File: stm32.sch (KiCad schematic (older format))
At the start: 46 parts, among them P1 USB_OTG, P2 CONN_01X04, U3 STM32F407VETx, U4 USBLC6-4SC6, Y2 25M

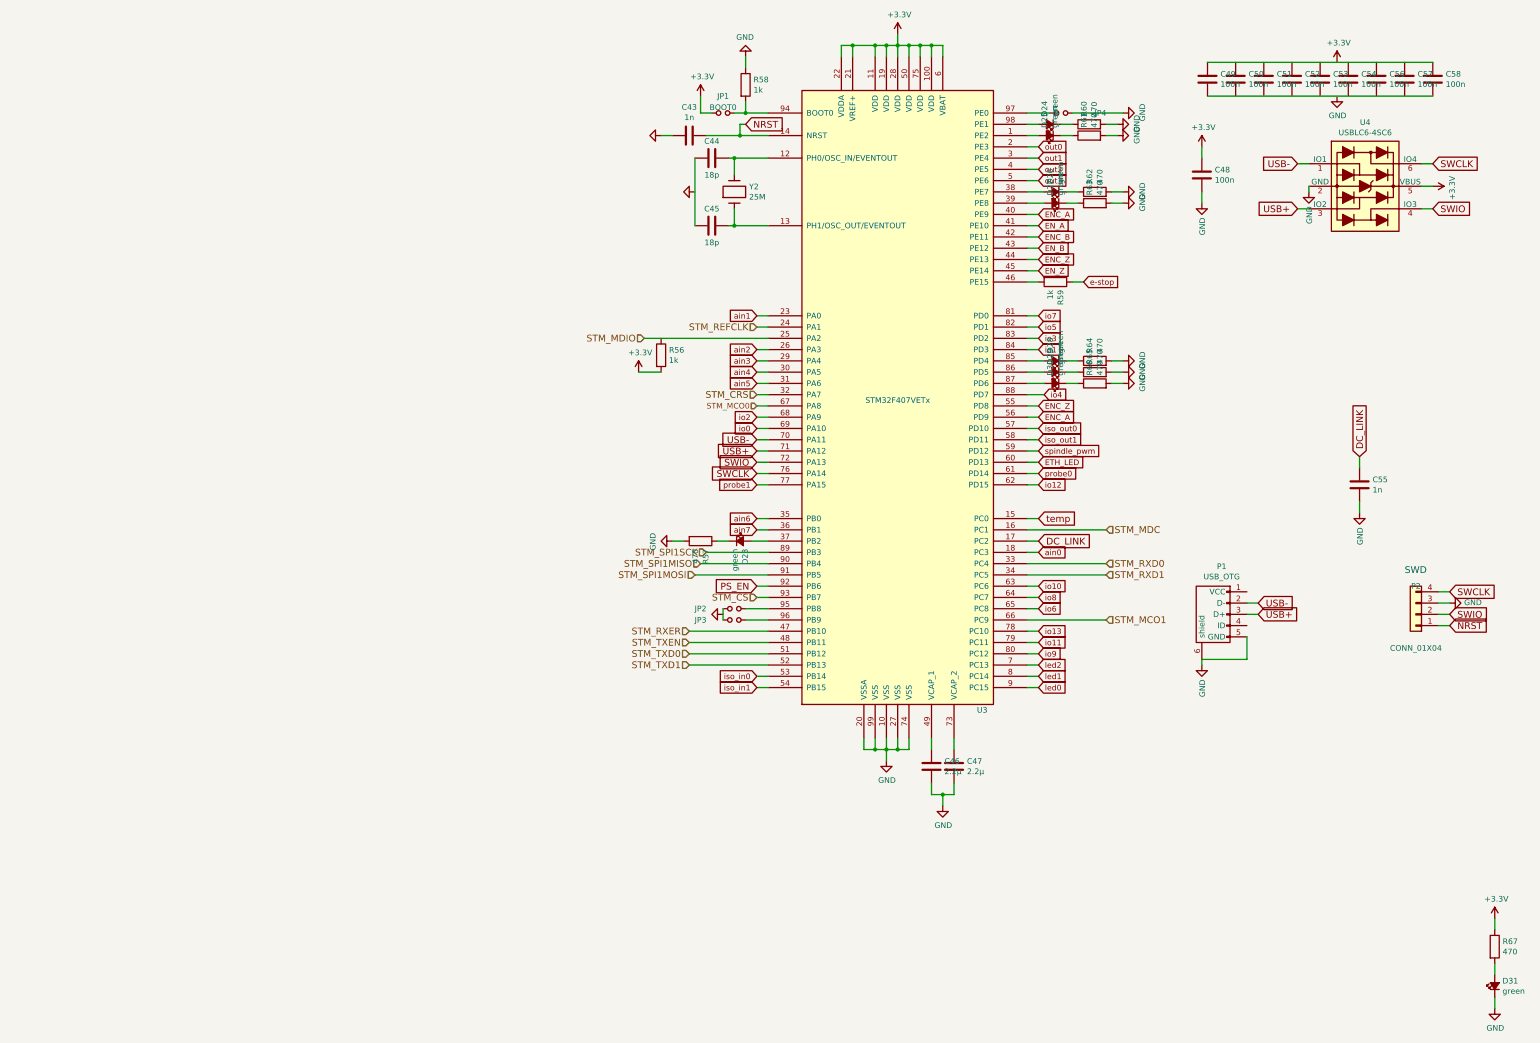
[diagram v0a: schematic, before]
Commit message: remove xfmrs from top board, no space with 18650 backup battery
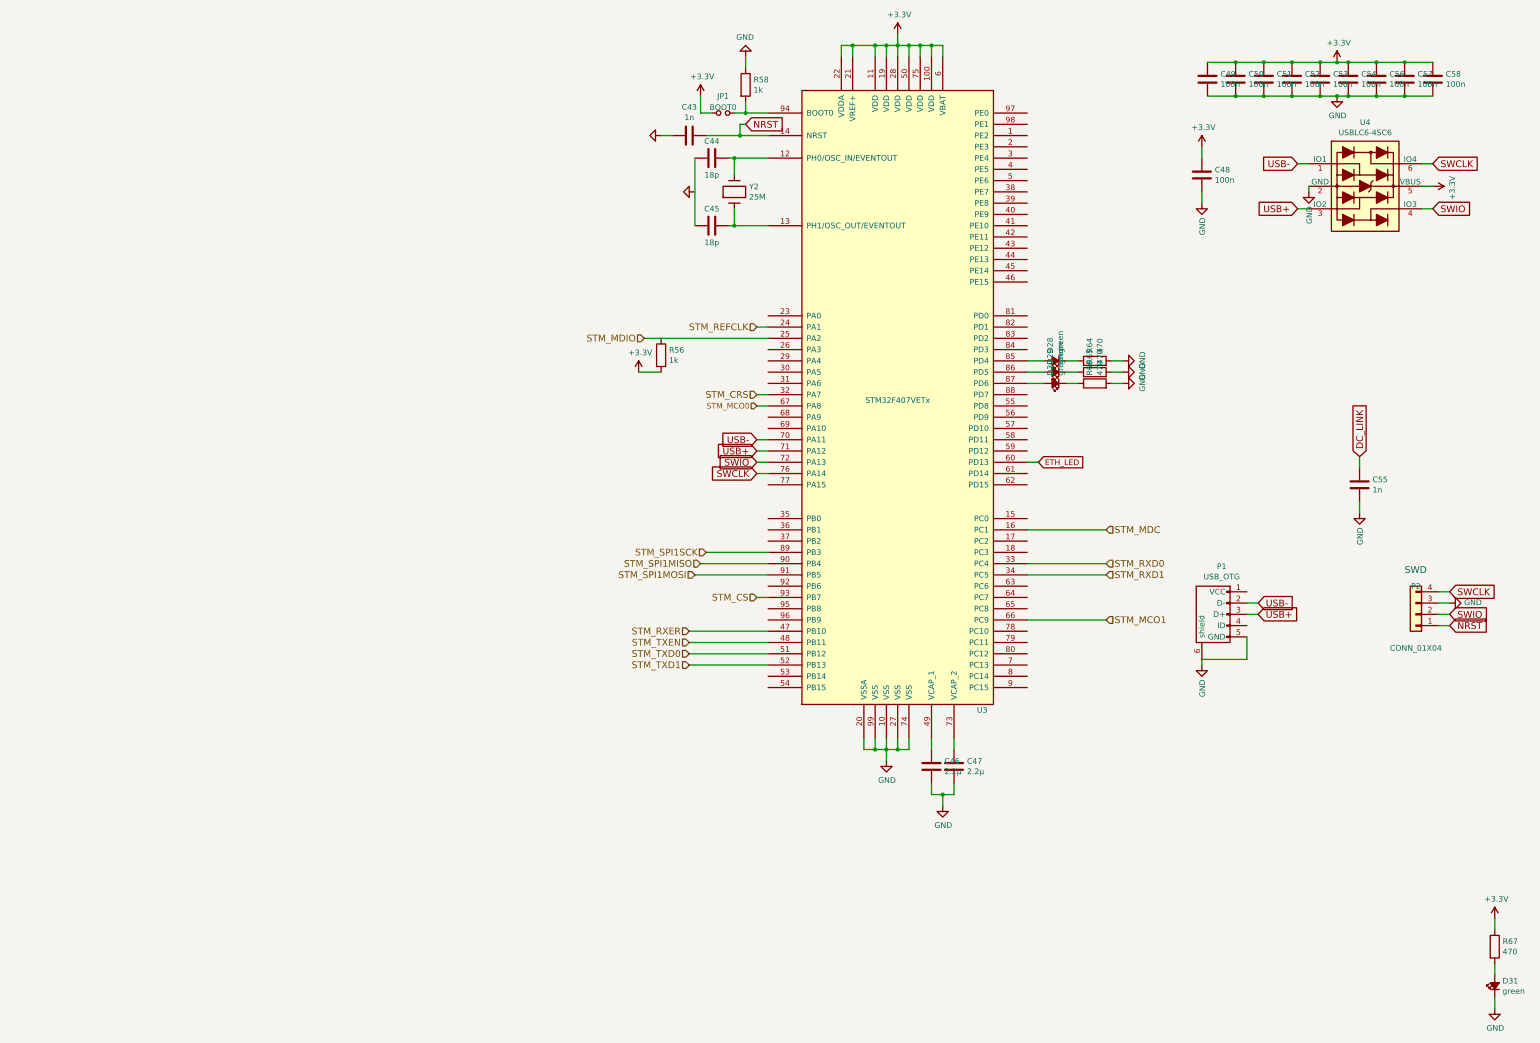
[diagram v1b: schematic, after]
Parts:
- removed D23, D24, D25, D26, D27: green, stmbl:LED-0805, symbol stmbl:Led_Small
- removed JP2, JP3, JP4: Jumper, stmbl:SOLDER_JUMPER, symbol stmbl:Jumper_NO_Small
- removed R57, R60, R61, R62, R63: 470, stmbl:R_0603, symbol stmbl:R
- removed R59: 1k, stmbl:R_0603, symbol stmbl:R
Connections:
- net +3V3: now also C49.2, C50.2, C51.2, C52.2, C53.2, C54.2, C56.2, C57.2, C58.2
- net DC_LINK: no longer U3.17 (PC2)
- net GND: now also C49.1, C50.1, C51.1, C52.1, C53.1, C54.1, C56.1, C57.1, C58.1
- net ENC_A: no longer names the net of U3.40 (PE9)
- net ENC_A: no longer U3.56 (PD9)
- net ENC_B: no longer names the net of U3.42 (PE11)
- net ENC_Z: no longer names the net of U3.44 (PE13)
- net ENC_Z: no longer U3.55 (PD8)
- net EN_A: no longer names the net of U3.41 (PE10)
- net EN_B: no longer names the net of U3.43 (PE12)
- net EN_Z: no longer names the net of U3.45 (PE14)
- net PS_EN: no longer names the net of U3.92 (PB6)
- net ain0: no longer names the net of U3.18 (PC3)
- net ain1: no longer names the net of U3.23 (PA0)
- net ain2: no longer names the net of U3.26 (PA3)
- net ain3: no longer names the net of U3.29 (PA4)
- net ain4: no longer names the net of U3.30 (PA5)
- net ain5: no longer names the net of U3.31 (PA6)
- net ain6: no longer names the net of U3.35 (PB0)
- net ain7: no longer names the net of U3.36 (PB1)
- net io0: no longer names the net of U3.69 (PA10)
- net io1: no longer names the net of U3.84 (PD3)
- net io10: no longer names the net of U3.63 (PC6)
- net io11: no longer names the net of U3.79 (PC11)
- net io12: no longer names the net of U3.62 (PD15)
- net io13: no longer names the net of U3.78 (PC10)
- net io2: no longer names the net of U3.68 (PA9)
- net io3: no longer names the net of U3.83 (PD2)
- net io4: no longer names the net of U3.88 (PD7)
- net io5: no longer names the net of U3.82 (PD1)
- net io6: no longer names the net of U3.65 (PC8)
- net io7: no longer names the net of U3.81 (PD0)
- net io8: no longer names the net of U3.64 (PC7)
- net io9: no longer names the net of U3.80 (PC12)
- net iso_in0: no longer names the net of U3.53 (PB14)
- net iso_in1: no longer names the net of U3.54 (PB15)
- net iso_out0: no longer names the net of U3.57 (PD10)
- net iso_out1: no longer names the net of U3.58 (PD11)
- net led0: no longer names the net of U3.9 (PC15)
- net led1: no longer names the net of U3.8 (PC14)
- net led2: no longer names the net of U3.7 (PC13)
- net out0: no longer names the net of U3.2 (PE3)
- net out1: no longer names the net of U3.3 (PE4)
- net out2: no longer names the net of U3.4 (PE5)
- net out3: no longer names the net of U3.5 (PE6)
- net probe0: no longer names the net of U3.61 (PD14)
- net probe1: no longer names the net of U3.77 (PA15)
- net spindle_pwm: no longer names the net of U3.59 (PD12)
- net temp: no longer names the net of U3.15 (PC0)

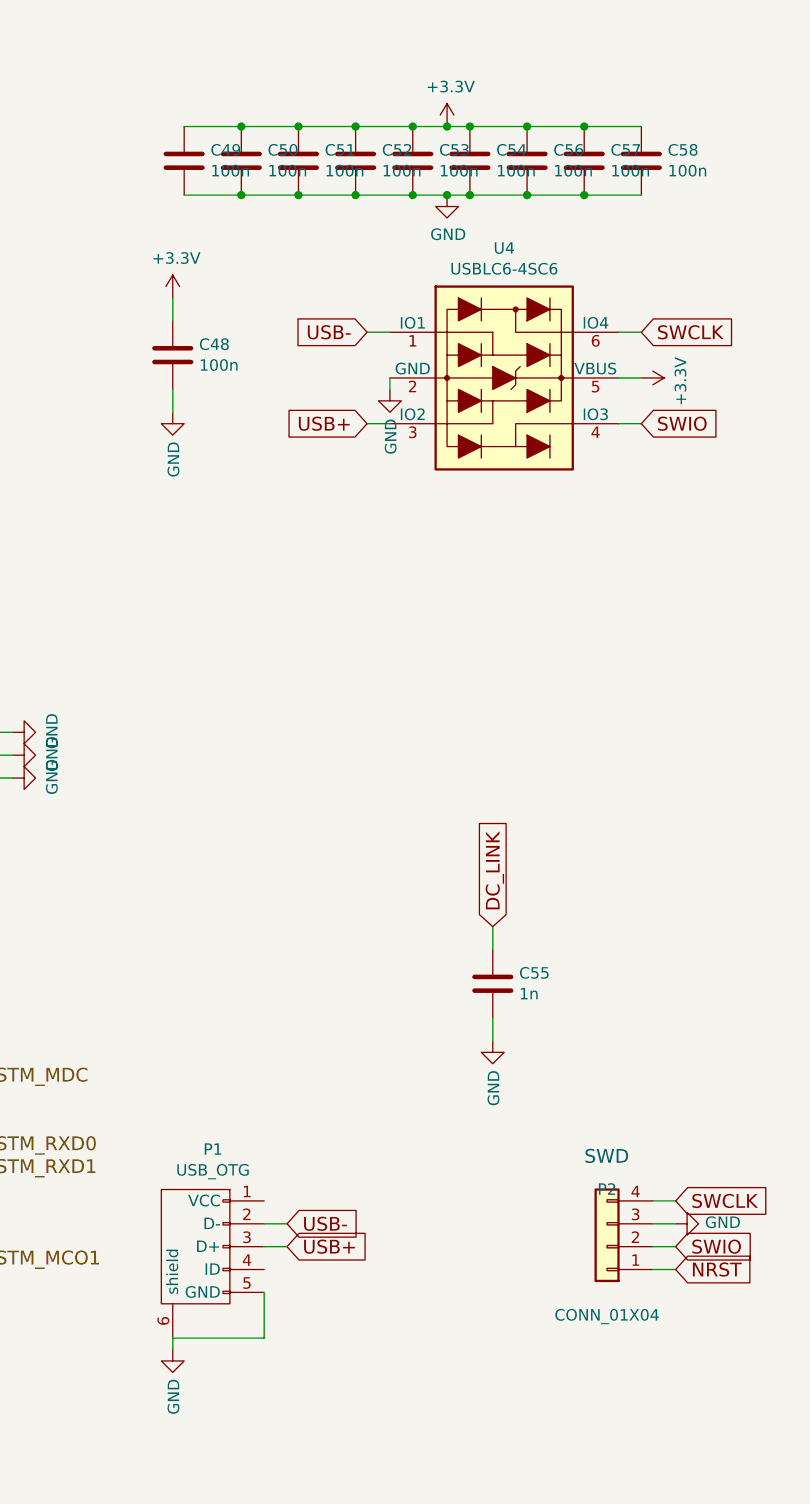
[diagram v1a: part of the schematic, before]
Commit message: Change to bigger housing
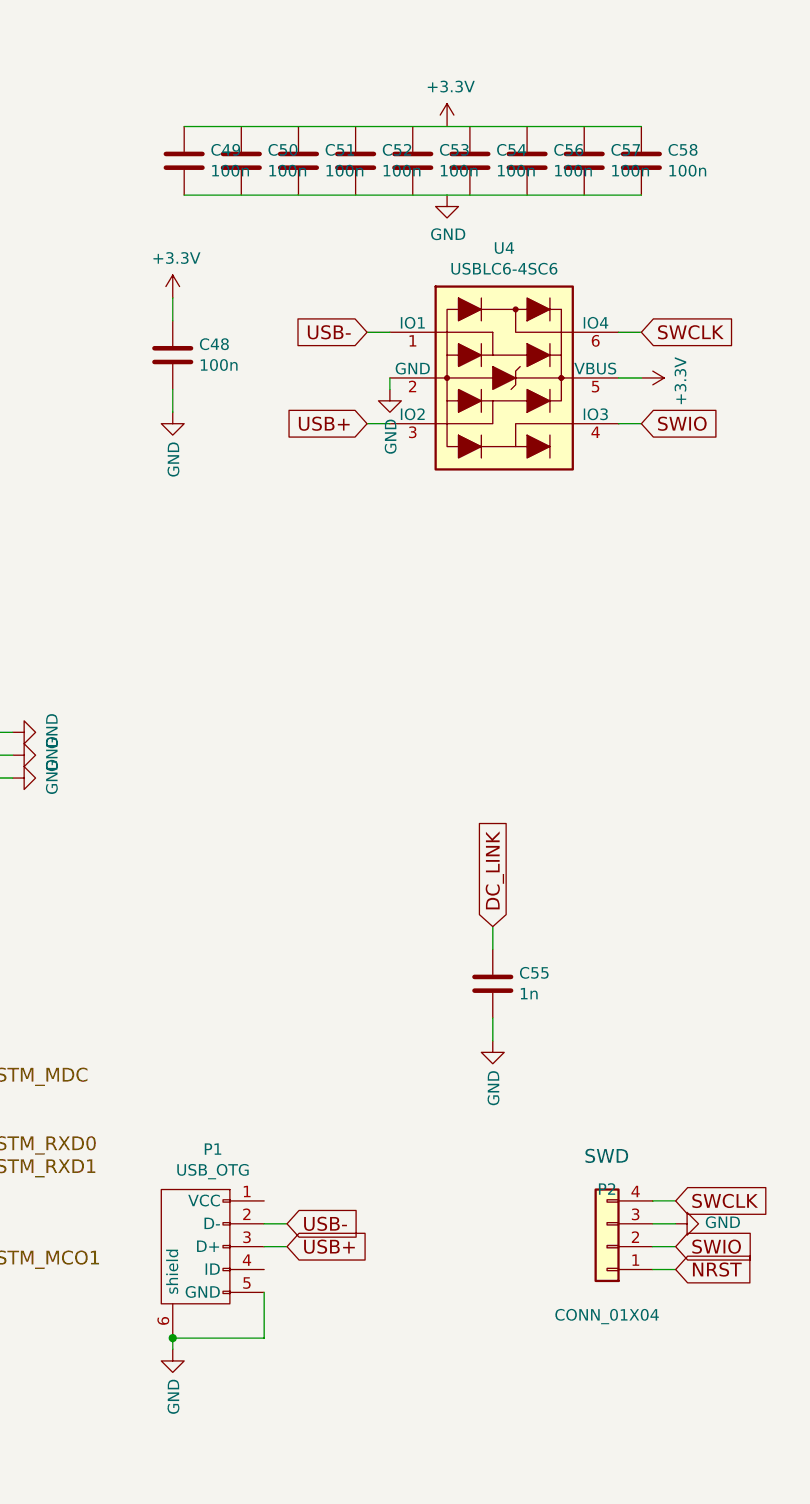
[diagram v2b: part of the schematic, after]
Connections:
- net +3V3: no longer C49.2, C50.2, C51.2, C52.2, C53.2, C54.2, C56.2, C57.2, C58.2
- net GND: no longer C49.1, C50.1, C51.1, C52.1, C53.1, C54.1, C56.1, C57.1, C58.1
- new net: C49.1, C58.1
- new net: C49.2, C58.2
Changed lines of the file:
@@
-EESchema Schematic File Version 4
+EESchema Schematic File Version 5
+LIBS:powermetering-cache
 EELAYER 29 0
 EELAYER END
@@
 	8300 1800 8300 2400
 Wire Wire Line
-	12850 950  13100 950
-Wire Wire Line
-	12850 1250 13100 1250
-Connection ~ 14600 950
-Wire Wire Line
-	14600 950  14850 950
-Connection ~ 14350 950
-Wire Wire Line
-	14350 950  14600 950
-Connection ~ 14100 950
-Wire Wire Line
-	14100 950  14350 950
-Connection ~ 14000 950
-Wire Wire Line
-	14000 950  14100 950
-Connection ~ 13850 950
-Wire Wire Line
-	13850 950  14000 950
-Connection ~ 13600 950
-Wire Wire Line
-	13600 950  13850 950
-Connection ~ 13350 950
-Wire Wire Line
-	13350 950  13600 950
-Connection ~ 13100 950
-Wire Wire Line
-	13100 950  13350 950
-Connection ~ 13100 1250
-Wire Wire Line
-	13100 1250 13350 1250
-Connection ~ 13350 1250
-Wire Wire Line
-	13350 1250 13600 1250
-Connection ~ 13600 1250
-Wire Wire Line
-	13600 1250 13850 1250
-Connection ~ 13850 1250
-Wire Wire Line
-	13850 1250 14000 1250
-Connection ~ 14000 1250
-Wire Wire Line
-	14000 1250 14100 1250
-Connection ~ 14100 1250
-Wire Wire Line
-	14100 1250 14350 1250
-Connection ~ 14350 1250
-Wire Wire Line
-	14350 1250 14600 1250
-Connection ~ 14600 1250
-Wire Wire Line
-	14600 1250 14850 1250
+	12850 1250 14850 1250
+Wire Wire Line
+	12850 950  14850 950
+Connection ~ 12800 6250
 $EndSCHEMATC

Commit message: add supply and AFE isolation
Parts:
- added Y3: RTC, stmbl:Crystal_SMD_0603_4Pads, symbol stmbl:Crystal
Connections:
- net +3V3: now also C49.2, C50.2, C51.2, C52.2, C53.2, C54.2, C56.2, C57.2, C58.2
- net GND: now also C49.1, C50.1, C51.1, C52.1, C53.1, C54.1, C56.1, C57.1, C58.1, Y3.1
- net STM_MDIO: now also R56.1
- net at U3.54 (PB15): now also Y3.2
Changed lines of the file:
@@
-EESchema Schematic File Version 5
+EESchema Schematic File Version 4
 LIBS:powermetering-cache
 EELAYER 29 0
@@
 $Descr A3 16535 11693
 encoding utf-8
-Sheet 3 4
+Sheet 3 3
 Title "STM32 Ethernet BOB"
 Date ""
@@
 Wire Wire Line
 	10400 900  10400 800
-Connection ~ 10400 800
-Wire Wire Line
-	10400 800  10500 800
 Wire Wire Line
 	10300 900  10300 800
@@
 	8400 5300 8950 5300
 Wire Wire Line
-	7850 3400 8950 3400
+	7850 3400 8000 3400
 Wire Wire Line
 	8300 1800 8300 2400
 Wire Wire Line
-	12850 1250 14850 1250
-Wire Wire Line
-	12850 950  14850 950
+	12850 1250 13100 1250
+Wire Wire Line
+	12850 950  13100 950
 Connection ~ 12800 6250
+$Comp
+L stmbl:Crystal Y3
+U 1 1 5D421BBB
+P 8950 6750
+F 0 "Y3" V 8996 6619 50  0000 R CNN
+F 1 "RTC" V 8905 6619 50  0000 R CNN
+F 2 "stmbl:Crystal_SMD_0603_4Pads" H 8950 6750 50  0001 C CNN
+F 3 "" H 8950 6750 50  0000 C CNN
+F 4 "LFXTAL061642Reel" H 300 4650 50  0001 C CNN "Manufacturer No"
+F 5 "Mouser 449-LFXTAL061642REEL" H 300 4650 50  0001 C CNN "Source"
+F 6 "" H 300 4650 50  0001 C CNN "Tolerance"
+F 7 "" H 300 4650 50  0001 C CNN "Voltage"
+	1    8950 6750
+	0    -1   -1   0
+$EndComp
+Wire Wire Line
+	8950 6500 8950 6600
+$Comp
+L stmbl:GND #PWR0161
+U 1 1 5D42CB08
+P 8950 7000
+F 0 "#PWR0161" H 8950 6750 50  0001 C CNN
+F 1 "GND" H 8955 6827 50  0000 C CNN
+F 2 "" H 8950 7000 50  0000 C CNN
+F 3 "" H 8950 7000 50  0000 C CNN
+	1    8950 7000
+	1    0    0    -1
+$EndComp
+Wire Wire Line
+	8950 7000 8950 6900
+Wire Wire Line
+	10500 800  10400 800
+Connection ~ 10400 800
+Connection ~ 14600 950
+Wire Wire Line
+	14600 950  14850 950
+Connection ~ 14350 950
+Wire Wire Line
+	14350 950  14600 950
+Connection ~ 14100 950
+Wire Wire Line
+	14100 950  14350 950
+Connection ~ 14000 950
+Wire Wire Line
+	14000 950  14100 950
+Connection ~ 13850 950
+Wire Wire Line
+	13850 950  14000 950
+Connection ~ 13600 950
+Wire Wire Line
+	13600 950  13850 950
+Connection ~ 13350 950
+Wire Wire Line
+	13350 950  13600 950
+Connection ~ 13100 950
+Wire Wire Line
+	13100 950  13350 950
+Connection ~ 13100 1250
+Wire Wire Line
+	13100 1250 13350 1250
+Connection ~ 13350 1250
+Wire Wire Line
+	13350 1250 13600 1250
+Connection ~ 13600 1250
+Wire Wire Line
+	13600 1250 13850 1250
+Connection ~ 13850 1250
+Wire Wire Line
+	13850 1250 14000 1250
+Connection ~ 14000 1250
+Wire Wire Line
+	14000 1250 14100 1250
+Connection ~ 14100 1250
+Wire Wire Line
+	14100 1250 14350 1250
+Connection ~ 14350 1250
+Wire Wire Line
+	14350 1250 14600 1250
+Connection ~ 14600 1250
+Wire Wire Line
+	14600 1250 14850 1250
+Connection ~ 8000 3400
+Wire Wire Line
+	8000 3400 8950 3400
 $EndSCHEMATC

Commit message: eth phy
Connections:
- net +3V3: now also D31.2 (A); no longer R67.1
- net GND: now also R67.2; no longer D31.1 (K)
- new net: D31.1 (K), R67.1
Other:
- moved on the sheet: D31, R67
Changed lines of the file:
@@
 L stmbl:Led_Small D31
 U 1 1 5B4CB472
-P 15400 9150
-F 0 "D31" V 15446 9082 50  0000 R CNN
-F 1 "green" V 15355 9082 50  0000 R CNN
-F 2 "stmbl:LED-0805" V 15400 9150 50  0001 C CNN
-F 3 "" V 15400 9150 50  0000 C CNN
-F 4 "LG R971" H 0   0   50  0001 C CNN "Manufacturer No"
-F 5 "Mouser 720-LGR971-KN-1" H 0   0   50  0001 C CNN "Source"
-F 6 "" H 0   0   50  0001 C CNN "Tolerance"
-F 7 "" H 0   0   50  0001 C CNN "Voltage"
-	1    15400 9150
+P 15400 8750
+F 0 "D31" V 15446 8682 50  0000 R CNN
+F 1 "green" V 15355 8682 50  0000 R CNN
+F 2 "stmbl:LED-0805" V 15400 8750 50  0001 C CNN
+F 3 "" V 15400 8750 50  0000 C CNN
+F 4 "LG R971" H 0   -400 50  0001 C CNN "Manufacturer No"
+F 5 "Mouser 720-LGR971-KN-1" H 0   -400 50  0001 C CNN "Source"
+F 6 "" H 0   -400 50  0001 C CNN "Tolerance"
+F 7 "" H 0   -400 50  0001 C CNN "Voltage"
+	1    15400 8750
 	0    -1   -1   0
 $EndComp
@@
 L stmbl:R R67
 U 1 1 5B4CB478
-P 15400 8800
-F 0 "R67" H 15470 8846 50  0000 L CNN
-F 1 "470" H 15470 8755 50  0000 L CNN
-F 2 "stmbl:R_0603" V 15330 8800 50  0001 C CNN
-F 3 "" H 15400 8800 50  0000 C CNN
-F 4 "" H 0   0   50  0001 C CNN "Manufacturer No"
-F 5 "" H 0   0   50  0001 C CNN "Source"
-F 6 "1%" H 0   0   50  0001 C CNN "Tolerance"
-F 7 "" H 0   0   50  0001 C CNN "Voltage"
-	1    15400 8800
+P 15400 9100
+F 0 "R67" H 15470 9146 50  0000 L CNN
+F 1 "470" H 15470 9055 50  0000 L CNN
+F 2 "stmbl:R_0603" V 15330 9100 50  0001 C CNN
+F 3 "" H 15400 9100 50  0000 C CNN
+F 4 "" H 0   300 50  0001 C CNN "Manufacturer No"
+F 5 "" H 0   300 50  0001 C CNN "Source"
+F 6 "1%" H 0   300 50  0001 C CNN "Tolerance"
+F 7 "" H 0   300 50  0001 C CNN "Voltage"
+	1    15400 9100
 	1    0    0    -1
 $EndComp
@@
 Wire Wire Line
 	11250 3600 11400 3600
-Wire Wire Line
-	15400 8950 15400 9050
 Text GLabel 14200 4450 1    60   Input ~ 0
 DC_LINK
@@
 Wire Wire Line
 	8000 3400 8950 3400
+Wire Wire Line
+	15400 8850 15400 8950
 $EndSCHEMATC
